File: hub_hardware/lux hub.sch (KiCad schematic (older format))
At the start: 27 parts, among them CON1 48V, CON2 USB-MINI-B, P7 CONN_4, Q1 DMP6023LE-13, SW1 BOOT, U1 3V3REG, U2 STM32F042-32, U3 4068

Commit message: kicad hardware files
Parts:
- added C13: 47n, SA0603, symbol C-RESCUE-lux_hub
- added C14: 100n, SA0603, symbol C-RESCUE-lux_hub
- added C15: 4u7, SA0603, symbol C-RESCUE-lux_hub
- C1: value C -> 100n; footprint (none) -> SA0603
- C2, C4: footprint (none) -> SA0805
- C3: footprint (none) -> C2V8
- C5, C6, R3, R4, R49, R5: footprint (none) -> SA0603
- CON1: footprint (none) -> BARREL_JACK
- CON2: footprint (none) -> USB_MINI_B
- D1, D15, D16, D2: footprint (none) -> SA0603_LED
- F1: footprint (none) -> FUSE5-20
- P7: footprint (none) -> SIL-4
- Q1, U1: footprint (none) -> SOT223
- R1: value R -> 100K; footprint (none) -> SA0603
- R2: value 4K7 -> 15K; footprint (none) -> SA0603
- R42: value R -> 120R; footprint (none) -> SA0603
- R50: value 10k -> 10K; footprint (none) -> SA0603
- SW1: footprint (none) -> TACT-SW-SMD
- U2: footprint MODULE -> LQFP32
- U3: footprint (none) -> SO14E
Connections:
- wire segments 94 -> 96
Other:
- note added: "P(Q1)~~0.5W"
- note added: "P(R2)=150mW"
- note added: "TC(R2,C3)=7s"
- note added: "Tss=10ms"
- moved on the sheet: C1, C3, C5, R2, R42

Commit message: Progress on v7 of led_strip_hardware; some lux utilities
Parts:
- C13: value 47n -> 100n
- C3: footprint C2V8 -> Discret:C2V8
- CON1: footprint BARREL_JACK -> Connect:BARREL_JACK
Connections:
- wire segments 96 -> 103
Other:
- note added: "Tss=20ms"
- note removed: "Tss=10ms"
- moved on the sheet: C3, R2

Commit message: Copper for the hub
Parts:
- removed SW1: BOOT, TACT-SW-SMD, symbol TACT
- added SW1: BOOT, SW_SPST_EVQPE1, symbol SW_PUSH
- C1, C13, C14, C5, C6: footprint SA0603 -> Capacitors_SMD:C_0402
- C15: footprint SA0603 -> Capacitors_SMD:C_0603
- C2, C4: footprint SA0805 -> Capacitors_SMD:C_0805
- D1, D15, D16, D2: footprint SA0603_LED -> LEDs:LED_0603
- R1, R4, R42, R49, R5: footprint SA0603 -> Resistors_SMD:R_0402
- R2, R3, R50: footprint SA0603 -> Resistors_SMD:R_0603
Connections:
- wire segments 103 -> 105
- no-connect marks 5 -> 3

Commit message: Hub gerbers; Reverting changes to lux API;
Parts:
- C15: footprint Capacitors_SMD:C_0603 -> Capacitors_SMD:C_0805
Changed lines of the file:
@@
 F 0 "C15" H 7050 4650 40  0000 L CNN
 F 1 "4u7" H 7056 4465 40  0000 L CNN
-F 2 "Capacitors_SMD:C_0603" H 7088 4400 30  0001 C CNN
+F 2 "Capacitors_SMD:C_0805" H 7088 4400 30  0001 C CNN
 F 3 "" H 7050 4550 60  0000 C CNN
 	1    7050 4550

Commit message: X11 -> lux bridge prototype
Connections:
- wire segments 105 -> 117
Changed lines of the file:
@@
 $EndComp
 Wire Wire Line
-	5450 1750 5450 2550
+	5450 1750 5450 2150
+Wire Wire Line
+	5450 2150 5450 2550
 $Comp
 L VDD #PWR06
@@
 $EndComp
 Wire Wire Line
-	1300 3250 1300 3950
+	1300 3250 1300 3400
+Wire Wire Line
+	1300 3400 1300 3700
+Wire Wire Line
+	1300 3700 1300 3850
+Wire Wire Line
+	1300 3850 1300 3950
 Connection ~ 1300 3400
 Connection ~ 1300 3700
@@
 	1600 2200 1700 2200
 Wire Wire Line
-	1700 2200 1700 2400
+	1700 2200 1700 2300
+Wire Wire Line
+	1700 2300 1700 2400
 Wire Wire Line
 	1700 2300 1600 2300
@@
 $EndComp
 Wire Wire Line
-	2850 1850 4000 1850
+	2850 1850 3250 1850
+Wire Wire Line
+	3250 1850 3650 1850
+Wire Wire Line
+	3650 1850 3900 1850
+Wire Wire Line
+	3900 1850 4000 1850
 $Comp
 L +48V #PWR026
@@
 	1700 1850 1750 1850
 Wire Wire Line
-	2250 1850 2450 1850
+	2250 1850 2350 1850
+Wire Wire Line
+	2350 1850 2450 1850
 $Comp
 L R-RESCUE-lux_hub R2
@@
 $EndComp
 Wire Wire Line
-	2350 2400 2700 2400
-Wire Wire Line
-	2650 2150 2650 2450
+	2350 2400 2650 2400
+Wire Wire Line
+	2650 2400 2700 2400
+Wire Wire Line
+	2650 2150 2650 2400
+Wire Wire Line
+	2650 2400 2650 2450
 Connection ~ 2650 2400
 Connection ~ 2350 2400
@@
 	3650 2400 3650 2450
 Wire Wire Line
-	3650 2450 3900 2450
+	3650 2450 3800 2450
+Wire Wire Line
+	3800 2450 3900 2450
 Wire Wire Line
 	3900 2450 3900 2350

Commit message: WIP Lux Hub v7
* Replace PTCs with current-limiting circuit
* Widen board and add 4x2mm mounting holes
* TODO: Rearrange some components on the edges
* TODO: Check silkscreen (esp. LEDs)
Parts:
- SW1: footprint SW_SPST_EVQPE1 -> Buttons_Switches_SMD:SW_SPST_EVQPE1
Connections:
- wire segments 117 -> 105
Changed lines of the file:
@@
 $EndComp
 Wire Wire Line
-	5450 1750 5450 2150
-Wire Wire Line
-	5450 2150 5450 2550
+	5450 1750 5450 2550
 $Comp
 L VDD #PWR06
@@
 $EndComp
 Wire Wire Line
-	1300 3250 1300 3400
-Wire Wire Line
-	1300 3400 1300 3700
-Wire Wire Line
-	1300 3700 1300 3850
-Wire Wire Line
-	1300 3850 1300 3950
+	1300 3250 1300 3950
 Connection ~ 1300 3400
 Connection ~ 1300 3700
@@
 	1600 2200 1700 2200
 Wire Wire Line
-	1700 2200 1700 2300
-Wire Wire Line
-	1700 2300 1700 2400
+	1700 2200 1700 2400
 Wire Wire Line
 	1700 2300 1600 2300
@@
 $EndComp
 Wire Wire Line
-	2850 1850 3250 1850
-Wire Wire Line
-	3250 1850 3650 1850
-Wire Wire Line
-	3650 1850 3900 1850
-Wire Wire Line
-	3900 1850 4000 1850
+	2850 1850 4000 1850
 $Comp
 L +48V #PWR026
@@
 	1700 1850 1750 1850
 Wire Wire Line
-	2250 1850 2350 1850
-Wire Wire Line
-	2350 1850 2450 1850
+	2250 1850 2450 1850
 $Comp
 L R-RESCUE-lux_hub R2
@@
 $EndComp
 Wire Wire Line
-	2350 2400 2650 2400
-Wire Wire Line
-	2650 2400 2700 2400
-Wire Wire Line
-	2650 2150 2650 2400
-Wire Wire Line
-	2650 2400 2650 2450
+	2350 2400 2700 2400
+Wire Wire Line
+	2650 2150 2650 2450
 Connection ~ 2650 2400
 Connection ~ 2350 2400
@@
 	3650 2400 3650 2450
 Wire Wire Line
-	3650 2450 3800 2450
-Wire Wire Line
-	3800 2450 3900 2450
+	3650 2450 3900 2450
 Wire Wire Line
 	3900 2450 3900 2350
@@
 F 0 "SW1" H 5050 1860 50  0000 C CNN
 F 1 "BOOT" H 4900 1670 50  0000 C CNN
-F 2 "SW_SPST_EVQPE1" H 4900 1600 50  0000 C CNN
+F 2 "Buttons_Switches_SMD:SW_SPST_EVQPE1" H 4900 1600 50  0000 C CNN
 F 3 "" H 4900 1750 50  0000 C CNN
 	1    4900 1750

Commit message: Lux Hub v8
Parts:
- removed C1, C13: 100n, Capacitors_SMD:C_0402, symbol C-RESCUE-lux_hub
- removed Q1: DMP6023LE-13, SOT223, symbol MOSFET_P
- removed R1: 100K, Resistors_SMD:R_0402, symbol R-RESCUE-lux_hub
- removed R42: 120R, Resistors_SMD:R_0402, symbol R-RESCUE-lux_hub
- C14, C5, C6: footprint Capacitors_SMD:C_0402 -> Capacitors_SMD:C_0603
- F1: footprint FUSE5-20 -> 0PTF0078P
- R4, R49, R5: footprint Resistors_SMD:R_0402 -> Resistors_SMD:R_0603
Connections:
- net labels added: PWR1, PWR2, PWR3, PWR4, PWR5, PWR6
- net labels removed: LED1, LED2, LED3, LED4, LED5, LED6
- wire segments 105 -> 97
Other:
- note removed: "P(Q1)~~0.5W"
- note removed: "Tss=20ms"

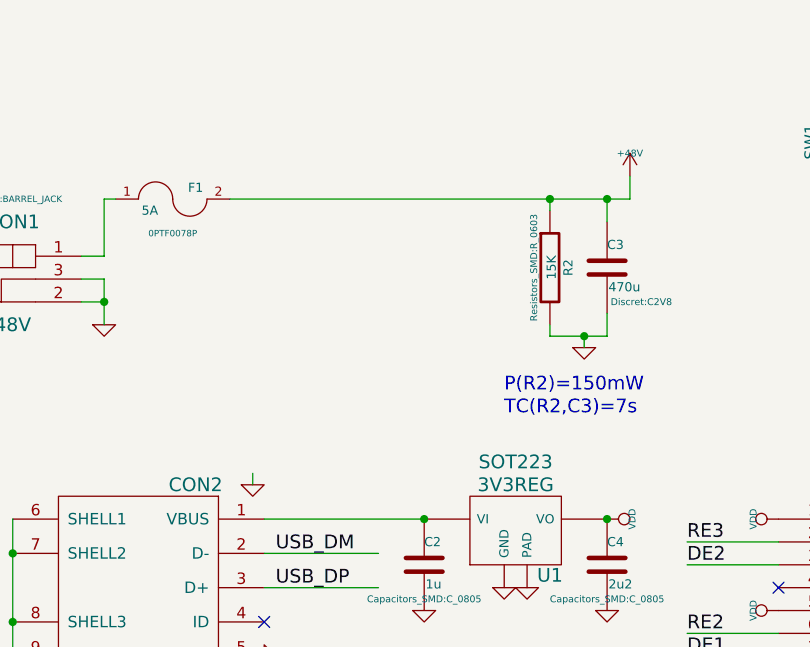
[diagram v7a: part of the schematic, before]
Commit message: Add soft-start circuit to lux hub v8, update gerbers
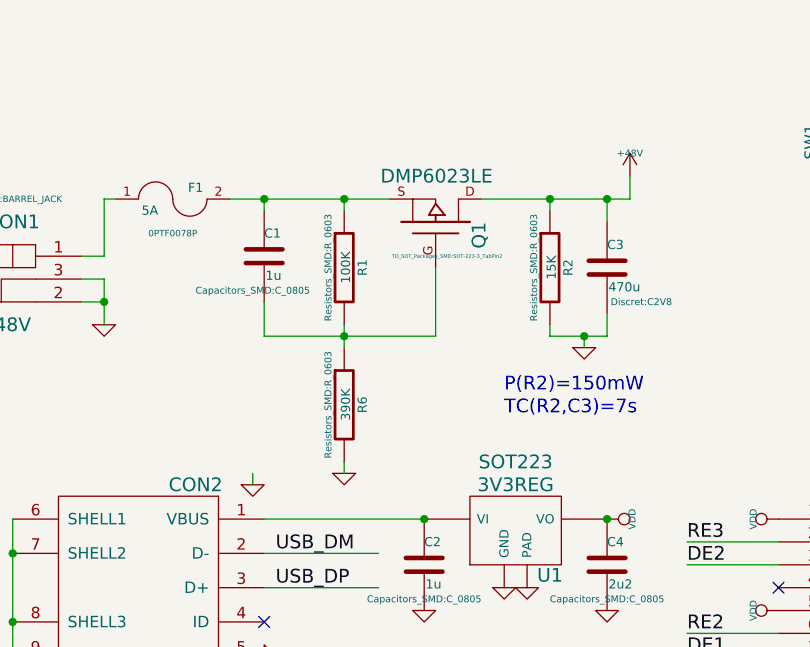
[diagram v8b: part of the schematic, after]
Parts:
- added C1: 1u, Capacitors_SMD:C_0805, symbol C-RESCUE-lux_hub
- added Q1: DMP6023LE, TO_SOT_Packages_SMD:SOT-223-3_TabPin2, symbol MOSFET_P
- added R1: 100K, Resistors_SMD:R_0603, symbol R-RESCUE-lux_hub
- added R6: 390K, Resistors_SMD:R_0603, symbol R-RESCUE-lux_hub
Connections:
- wire segments 97 -> 105
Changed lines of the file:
@@
 	8450 1750 8700 1750
 Wire Wire Line
-	2250 1850 4000 1850
+	3350 1850 4000 1850
+$Comp
+L MOSFET_P Q1
+U 1 1 5AFCDAEA
+P 3150 1950
+F 0 "Q1" H 3150 2140 60  0000 R CNN
+F 1 "DMP6023LE" V 3350 2200 60  0000 R CNN
+F 2 "TO_SOT_Packages_SMD:SOT-223-3_TabPin2" V 3000 2000 16  0000 C CNN
+F 3 "" H 3150 1950 60  0000 C CNN
+	1    3150 1950
+	0    1    -1   0
+$EndComp
+$Comp
+L R-RESCUE-lux_hub R1
+U 1 1 5AFCE142
+P 2750 2150
+F 0 "R1" V 2830 2150 40  0000 C CNN
+F 1 "100K" V 2757 2151 40  0000 C CNN
+F 2 "Resistors_SMD:R_0603" V 2680 2150 30  0000 C CNN
+F 3 "" H 2750 2150 30  0000 C CNN
+	1    2750 2150
+	1    0    0    -1
+$EndComp
+$Comp
+L R-RESCUE-lux_hub R6
+U 1 1 5AFCE310
+P 2750 2750
+F 0 "R6" V 2830 2750 40  0000 C CNN
+F 1 "390K" V 2757 2751 40  0000 C CNN
+F 2 "Resistors_SMD:R_0603" V 2680 2750 30  0000 C CNN
+F 3 "" H 2750 2750 30  0000 C CNN
+	1    2750 2750
+	1    0    0    -1
+$EndComp
+$Comp
+L GND-RESCUE-lux_hub #PWR039
+U 1 1 5AFCE530
+P 2750 3050
+F 0 "#PWR039" H 2750 3050 30  0001 C CNN
+F 1 "GND" H 2750 2980 30  0001 C CNN
+F 2 "" H 2750 3050 60  0000 C CNN
+F 3 "" H 2750 3050 60  0000 C CNN
+	1    2750 3050
+	1    0    0    -1
+$EndComp
+Wire Wire Line
+	2750 3050 2750 3000
+Wire Wire Line
+	2750 2400 2750 2500
+Wire Wire Line
+	2400 2450 3150 2450
+Wire Wire Line
+	3150 2450 3150 2150
+Connection ~ 2750 2450
+Wire Wire Line
+	2750 1900 2750 1850
+Wire Wire Line
+	2250 1850 2950 1850
+Connection ~ 2750 1850
+$Comp
+L C-RESCUE-lux_hub C1
+U 1 1 5AFCF05A
+P 2400 2100
+F 0 "C1" H 2400 2200 40  0000 L CNN
+F 1 "1u" H 2406 2015 40  0000 L CNN
+F 2 "Capacitors_SMD:C_0805" H 2350 1950 30  0000 C CNN
+F 3 "" H 2400 2100 60  0000 C CNN
+	1    2400 2100
+	1    0    0    -1
+$EndComp
+Wire Wire Line
+	2400 1850 2400 1900
+Connection ~ 2400 1850
+Wire Wire Line
+	2400 2300 2400 2450
 $EndSCHEMATC
